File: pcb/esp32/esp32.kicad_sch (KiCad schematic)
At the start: 15 parts, among them J1 Conn_01x02_Female, J2 Conn_01x15_Female, J3 Screw_Terminal_01x02, J4 Conn_01x15_Female, J5 Conn_01x15_Female, J6 Conn_01x02_Female, J6der1 Conn_01x15_Female, J7 Conn_01x02_Female, J7der1 Conn_01x15_Female, J8 Conn_01x02_Female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

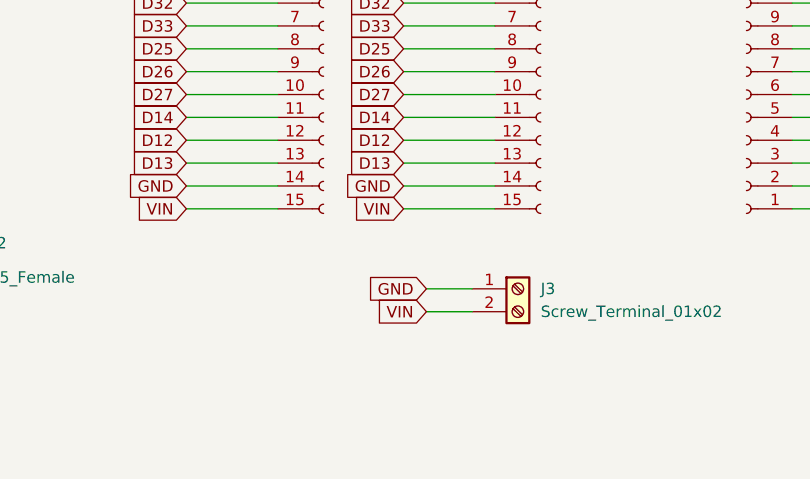
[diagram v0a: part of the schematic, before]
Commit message: added diode to esp32 board and updated solar board to fixed 5.0v ams1117
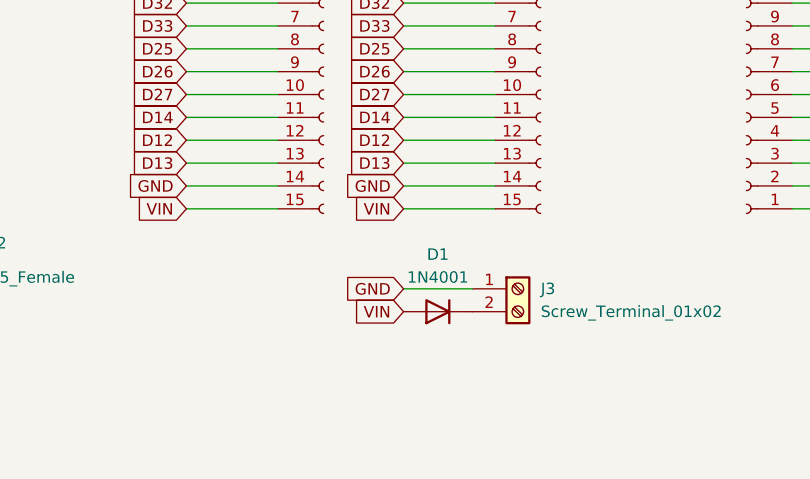
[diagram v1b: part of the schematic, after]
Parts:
- added D1: 1N4001, Diode_THT:D_DO-41_SOD81_P10.16mm_Horizontal, symbol Diode:1N4001
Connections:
- net VIN: now also D1.2 (A); no longer J3.2 (Pin_2)
- new net: D1.1 (K), J3.2 (Pin_2)
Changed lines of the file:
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@@
     (stroke (width 0) (type default) (color 0 0 0 0))
   )
-  (wire (pts (xy 121.92 97.79) (xy 127 97.79))
+  (wire (pts (xy 119.38 97.79) (xy 127 97.79))
     (stroke (width 0) (type default) (color 0 0 0 0))
   )
@@
     (stroke (width 0) (type default) (color 0 0 0 0))
   )
-  (wire (pts (xy 121.92 100.33) (xy 127 100.33))
-    (stroke (width 0) (type default) (color 0 0 0 0))
-  )
   (wire (pts (xy 57.15 63.5) (xy 67.31 63.5))
     (stroke (width 0) (type default) (color 0 0 0 0))
@@
     )
   )
-  (global_label "GND" (shape input) (at 121.92 97.79 180) (fields_autoplaced)
-    (effects (font (size 1.27 1.27)) (justify right))
-    (property "Intersheet References" "${INTERSHEET_REFS}" (id 0) (at 115.6364 97.7106 0)
+  (global_label "GND" (shape input) (at 119.38 97.79 180) (fields_autoplaced)
+    (effects (font (size 1.27 1.27)) (justify right))
+    (property "Intersheet References" "${INTERSHEET_REFS}" (id 0) (at 113.0964 97.7106 0)
       (effects (font (size 1.27 1.27)) (justify right) hide)
     )
@@
     )
   )
-  (global_label "VIN" (shape input) (at 121.92 100.33 180) (fields_autoplaced)
-    (effects (font (size 1.27 1.27)) (justify right))
-    (property "Intersheet References" "${INTERSHEET_REFS}" (id 0) (at 116.4831 100.2506 0)
+  (global_label "VIN" (shape input) (at 119.38 100.33 180) (fields_autoplaced)
+    (effects (font (size 1.27 1.27)) (justify right))
+    (property "Intersheet References" "${INTERSHEET_REFS}" (id 0) (at 113.9431 100.2506 0)
       (effects (font (size 1.27 1.27)) (justify right) hide)
     )
@@
     (pin "9")
   )
+  (symbol (lib_id "Diode:1N4001") (at 123.19 100.33 180) (unit 1)
+    (in_bom yes) (on_board yes) (fields_autoplaced)
+    (property "Reference" "D1" (id 0) (at 123.19 93.98 0))
+    (property "Value" "1N4001" (id 1) (at 123.19 96.52 0))
+    (property "Footprint" "Diode_THT:D_DO-41_SOD81_P10.16mm_Horizontal" (id 2) (at 123.19 95.885 0)
+      (effects (font (size 1.27 1.27)) hide)
+    )
+    (property "Datasheet" "http://www.vishay.com/docs/88503/1n4001.pdf" (id 3) (at 123.19 100.33 0)
+      (effects (font (size 1.27 1.27)) hide)
+    )
+    (pin "1")
+    (pin "2")
+  )
   (symbol (lib_id "Mechanical:MountingHole") (at 254 110.49 0) (unit 1)
     (in_bom yes) (on_board yes) (fields_autoplaced)
@@
   )
   (symbol_instances
+    (path "/5f59c1b8-50da-47fc-86f1-8013e6be9ffb"
+      (reference "D1") (unit 1) (value "1N4001") (footprint "Diode_THT:D_DO-41_SOD81_P10.16mm_Horizontal")
+    )
     (path "/90e39933-8cf6-43e9-82d7-37665a3a8f34"
       (reference "H1") (unit 1) (value "MountingHole") (footprint "MountingHole:MountingHole_2.1mm")

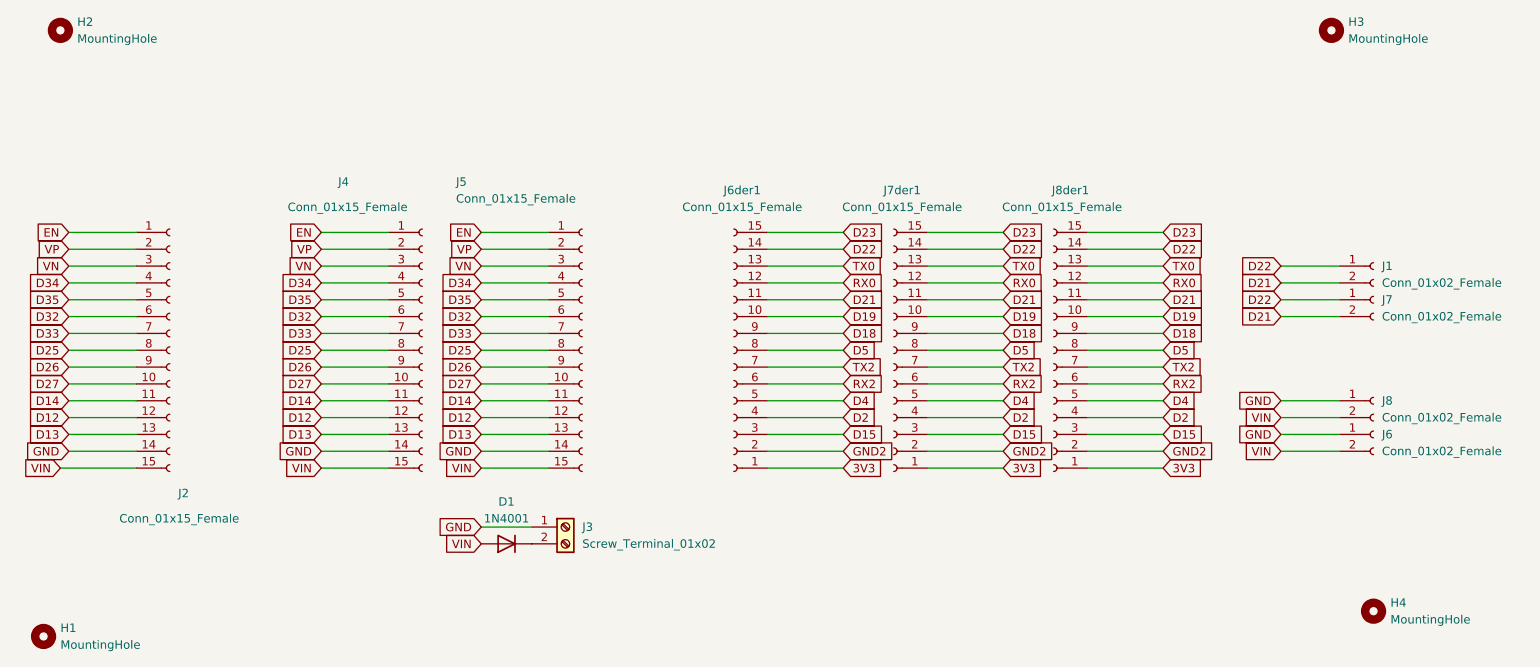
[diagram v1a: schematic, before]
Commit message: added new pins to connect more 3.3v sensors and 5.0v sensors, also added 2 pull up resistors for sda and scl pins
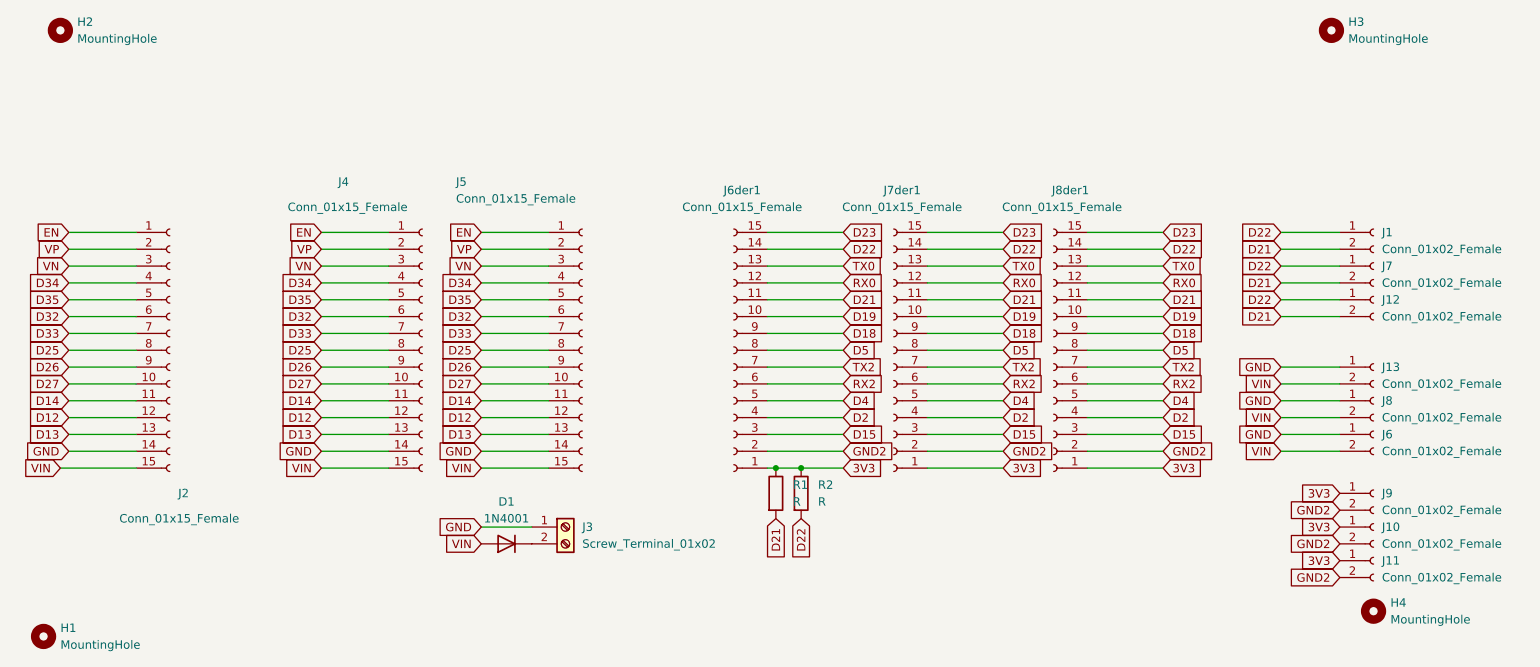
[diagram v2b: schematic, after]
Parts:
- added J10, J11, J12, J13, J9: Conn_01x02_Female, esp32_ur:Connector_Molex_Molex_SL_171971-0004_1x02_P2.54mm_Vertical_squares, symbol Connector:Conn_01x02_Female
- added R1: R, Resistor_THT:R_Axial_DIN0204_L3.6mm_D1.6mm_P5.08mm_Horizontal, symbol Device:R
- added R2: R, Resistor_THT:R_Axial_DIN0204_L3.6mm_D1.6mm_P7.62mm_Horizontal, symbol Device:R
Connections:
- net 3V3: now also J10.1 (Pin_1), J11.1 (Pin_1), J9.1 (Pin_1), R1.1, R2.1
- net D21: now also J12.2 (Pin_2), R1.2
- net D22: now also J12.1 (Pin_1), R2.2
- net GND: now also J13.1 (Pin_1)
- net GND2: now also J10.2 (Pin_2), J11.2 (Pin_2), J9.2 (Pin_2)
- net VIN: now also J13.2 (Pin_2)
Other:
- moved on the sheet: J1, J7

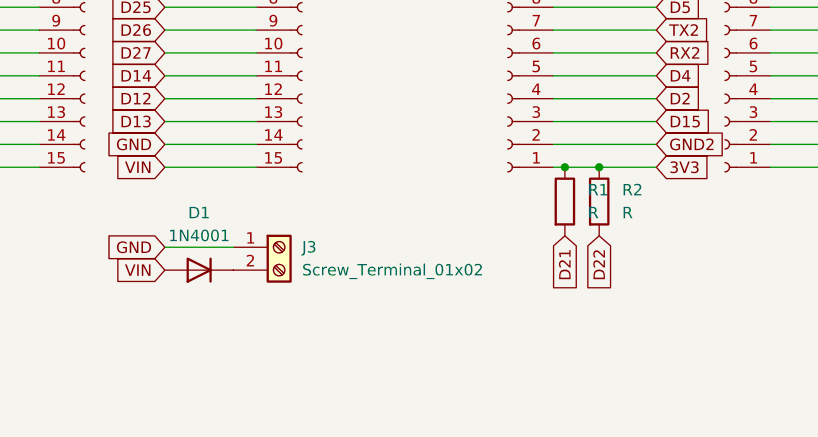
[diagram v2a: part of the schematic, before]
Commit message: changed the pull up from 5v to 3.3v
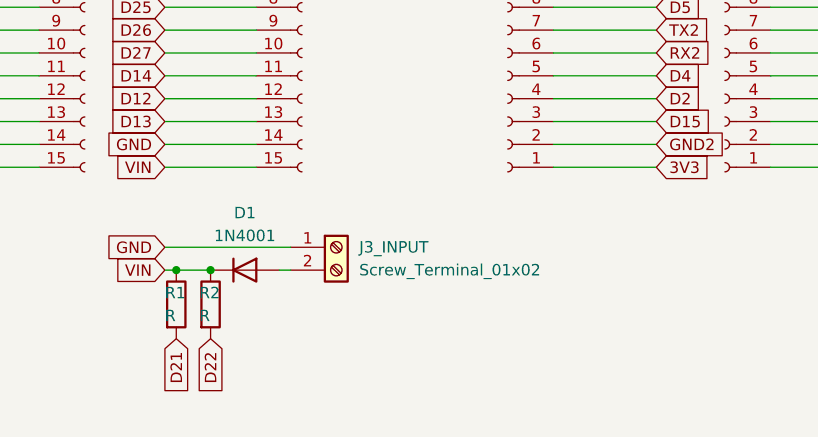
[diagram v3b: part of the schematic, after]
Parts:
- R1: footprint Resistor_THT:R_Axial_DIN0204_L3.6mm_D1.6mm_P5.08mm_Horizontal -> Resistor_THT:R_Axial_DIN0207_L6.3mm_D2.5mm_P15.24mm_Horizontal
- renumbered J3 to J3_INPUT
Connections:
- net 3V3: no longer R1.1, R2.1
- net VIN: now also D1.1 (K), R1.1, R2.1; no longer D1.2 (A)
- net at J3_INPUT.2 (Pin_2): now also D1.2 (A); no longer D1.1 (K)
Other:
- moved on the sheet: D1, J3_INPUT, R1, R2
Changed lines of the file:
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@@
 (kicad_sch (version 20211123) (generator eeschema)
   (paper "A4")
-  (junction (at 167.64 88.9) (diameter 0) (color 0 0 0 0)
-  )
-  (junction (at 163.83 88.9) (diameter 0) (color 0 0 0 0)
+  (junction (at 120.65 100.33) (diameter 0) (color 0 0 0 0)
+  )
+  (junction (at 124.46 100.33) (diameter 0) (color 0 0 0 0)
   )
   (wire (pts (xy 240.03 60.96) (xy 248.92 60.96))
@@
     (stroke (width 0) (type default) (color 0 0 0 0))
   )
-  (wire (pts (xy 162.56 88.9) (xy 163.83 88.9))
-    (stroke (width 0) (type default) (color 0 0 0 0))
-  )
   (wire (pts (xy 57.15 73.66) (xy 67.31 73.66))
     (stroke (width 0) (type default) (color 0 0 0 0))
@@
     (stroke (width 0) (type default) (color 0 0 0 0))
   )
+  (wire (pts (xy 120.65 100.33) (xy 124.46 100.33))
+    (stroke (width 0) (type default) (color 0 0 0 0))
+  )
   (wire (pts (xy 162.56 66.04) (xy 173.99 66.04))
     (stroke (width 0) (type default) (color 0 0 0 0))
@@
     (stroke (width 0) (type default) (color 0 0 0 0))
   )
-  (wire (pts (xy 119.38 97.79) (xy 127 97.79))
+  (wire (pts (xy 119.38 97.79) (xy 133.35 97.79))
     (stroke (width 0) (type default) (color 0 0 0 0))
   )
@@
     (stroke (width 0) (type default) (color 0 0 0 0))
   )
+  (wire (pts (xy 119.38 100.33) (xy 120.65 100.33))
+    (stroke (width 0) (type default) (color 0 0 0 0))
+  )
+  (wire (pts (xy 132.08 100.33) (xy 133.35 100.33))
+    (stroke (width 0) (type default) (color 0 0 0 0))
+  )
   (wire (pts (xy 119.38 76.2) (xy 129.54 76.2))
     (stroke (width 0) (type default) (color 0 0 0 0))
@@
     (stroke (width 0) (type default) (color 0 0 0 0))
   )
-  (wire (pts (xy 163.83 88.9) (xy 167.64 88.9))
-    (stroke (width 0) (type default) (color 0 0 0 0))
-  )
   (wire (pts (xy 119.38 73.66) (xy 129.54 73.66))
     (stroke (width 0) (type default) (color 0 0 0 0))
@@
     (stroke (width 0) (type default) (color 0 0 0 0))
   )
-  (wire (pts (xy 167.64 88.9) (xy 173.99 88.9))
+  (wire (pts (xy 162.56 88.9) (xy 173.99 88.9))
     (stroke (width 0) (type default) (color 0 0 0 0))
   )
@@
     )
   )
-  (global_label "D21" (shape input) (at 163.83 96.52 270) (fields_autoplaced)
-    (effects (font (size 1.27 1.27)) (justify right))
-    (property "Intersheet References" "${INTERSHEET_REFS}" (id 0) (at 163.9094 102.6221 90)
+  (global_label "D21" (shape input) (at 120.65 107.95 270) (fields_autoplaced)
+    (effects (font (size 1.27 1.27)) (justify right))
+    (property "Intersheet References" "${INTERSHEET_REFS}" (id 0) (at 120.7294 114.0521 90)
       (effects (font (size 1.27 1.27)) (justify right) hide)
     )
@@
     )
   )
-  (global_label "D22" (shape input) (at 167.64 96.52 270) (fields_autoplaced)
-    (effects (font (size 1.27 1.27)) (justify right))
-    (property "Intersheet References" "${INTERSHEET_REFS}" (id 0) (at 167.7194 102.6221 90)
+  (global_label "D22" (shape input) (at 124.46 107.95 270) (fields_autoplaced)
+    (effects (font (size 1.27 1.27)) (justify right))
+    (property "Intersheet References" "${INTERSHEET_REFS}" (id 0) (at 124.5394 114.0521 90)
       (effects (font (size 1.27 1.27)) (justify right) hide)
     )
@@
     (pin "9")
   )
-  (symbol (lib_id "Diode:1N4001") (at 123.19 100.33 180) (unit 1)
+  (symbol (lib_id "Diode:1N4001") (at 128.27 100.33 0) (unit 1)
     (in_bom yes) (on_board yes) (fields_autoplaced)
-    (property "Reference" "D1" (id 0) (at 123.19 93.98 0))
-    (property "Value" "1N4001" (id 1) (at 123.19 96.52 0))
-    (property "Footprint" "Diode_THT:D_DO-41_SOD81_P10.16mm_Horizontal" (id 2) (at 123.19 95.885 0)
-      (effects (font (size 1.27 1.27)) hide)
-    )
-    (property "Datasheet" "http://www.vishay.com/docs/88503/1n4001.pdf" (id 3) (at 123.19 100.33 0)
+    (property "Reference" "D1" (id 0) (at 128.27 93.98 0))
+    (property "Value" "1N4001" (id 1) (at 128.27 96.52 0))
+    (property "Footprint" "Diode_THT:D_DO-41_SOD81_P10.16mm_Horizontal" (id 2) (at 128.27 104.775 0)
+      (effects (font (size 1.27 1.27)) hide)
+    )
+    (property "Datasheet" "http://www.vishay.com/docs/88503/1n4001.pdf" (id 3) (at 128.27 100.33 0)
       (effects (font (size 1.27 1.27)) hide)
     )
@@
     )
   )
-  (symbol (lib_id "Device:R") (at 167.64 92.71 0) (unit 1)
-    (in_bom yes) (on_board yes) (fields_autoplaced)
-    (property "Reference" "R2" (id 0) (at 170.18 91.4399 0)
-      (effects (font (size 1.27 1.27)) (justify left))
-    )
-    (property "Value" "R" (id 1) (at 170.18 93.9799 0)
-      (effects (font (size 1.27 1.27)) (justify left))
-    )
-    (property "Footprint" "Resistor_THT:R_Axial_DIN0204_L3.6mm_D1.6mm_P7.62mm_Horizontal" (id 2) (at 165.862 92.71 90)
-      (effects (font (size 1.27 1.27)) hide)
-    )
-    (property "Datasheet" "~" (id 3) (at 167.64 92.71 0)
+  (symbol (lib_id "Device:R") (at 124.46 104.14 0) (unit 1)
+    (in_bom yes) (on_board yes)
+    (property "Reference" "R2" (id 0) (at 123.19 102.87 0)
+      (effects (font (size 1.27 1.27)) (justify left))
+    )
+    (property "Value" "R" (id 1) (at 123.19 105.41 0)
+      (effects (font (size 1.27 1.27)) (justify left))
+    )
+    (property "Footprint" "Resistor_THT:R_Axial_DIN0204_L3.6mm_D1.6mm_P7.62mm_Horizontal" (id 2) (at 122.682 104.14 90)
+      (effects (font (size 1.27 1.27)) hide)
+    )
+    (property "Datasheet" "~" (id 3) (at 124.46 104.14 0)
       (effects (font (size 1.27 1.27)) hide)
     )
@@
     (pin "2")
   )
-  (symbol (lib_id "Device:R") (at 163.83 92.71 0) (unit 1)
-    (in_bom yes) (on_board yes) (fields_autoplaced)
-    (property "Reference" "R1" (id 0) (at 166.37 91.4399 0)
-      (effects (font (size 1.27 1.27)) (justify left))
-    )
-    (property "Value" "R" (id 1) (at 166.37 93.9799 0)
-      (effects (font (size 1.27 1.27)) (justify left))
-    )
-    (property "Footprint" "Resistor_THT:R_Axial_DIN0204_L3.6mm_D1.6mm_P5.08mm_Horizontal" (id 2) (at 162.052 92.71 90)
-      (effects (font (size 1.27 1.27)) hide)
-    )
-    (property "Datasheet" "~" (id 3) (at 163.83 92.71 0)
+  (symbol (lib_id "Device:R") (at 120.65 104.14 0) (unit 1)
+    (in_bom yes) (on_board yes)
+    (property "Reference" "R1" (id 0) (at 119.38 102.87 0)
+      (effects (font (size 1.27 1.27)) (justify left))
+    )
+    (property "Value" "R" (id 1) (at 119.38 105.41 0)
+      (effects (font (size 1.27 1.27)) (justify left))
+    )
+    (property "Footprint" "Resistor_THT:R_Axial_DIN0207_L6.3mm_D2.5mm_P15.24mm_Horizontal" (id 2) (at 118.872 104.14 90)
+      (effects (font (size 1.27 1.27)) hide)
+    )
+    (property "Datasheet" "~" (id 3) (at 120.65 104.14 0)
       (effects (font (size 1.27 1.27)) hide)
     )
@@
     )
   )
-  (symbol (lib_id "Connector:Screw_Terminal_01x02") (at 132.08 97.79 0) (unit 1)
+  (symbol (lib_id "Connector:Screw_Terminal_01x02") (at 138.43 97.79 0) (unit 1)
     (in_bom yes) (on_board yes) (fields_autoplaced)
-    (property "Reference" "J3" (id 0) (at 134.62 97.7899 0)
-      (effects (font (size 1.27 1.27)) (justify left))
-    )
-    (property "Value" "Screw_Terminal_01x02" (id 1) (at 134.62 100.3299 0)
-      (effects (font (size 1.27 1.27)) (justify left))
-    )
-    (property "Footprint" "TerminalBlock_MetzConnect:TerminalBlock_MetzConnect_Type055_RT01502HDWU_1x02_P5.00mm_Horizontal" (id 2) (at 132.08 97.79 0)
-      (effects (font (size 1.27 1.27)) hide)
-    )
-    (property "Datasheet" "~" (id 3) (at 132.08 97.79 0)
+    (property "Reference" "J3_INPUT" (id 0) (at 140.97 97.7899 0)
+      (effects (font (size 1.27 1.27)) (justify left))
+    )
+    (property "Value" "Screw_Terminal_01x02" (id 1) (at 140.97 100.3299 0)
+      (effects (font (size 1.27 1.27)) (justify left))
+    )
+    (property "Footprint" "TerminalBlock_MetzConnect:TerminalBlock_MetzConnect_Type055_RT01502HDWU_1x02_P5.00mm_Horizontal" (id 2) (at 138.43 97.79 0)
+      (effects (font (size 1.27 1.27)) hide)
+    )
+    (property "Datasheet" "~" (id 3) (at 138.43 97.79 0)
       (effects (font (size 1.27 1.27)) hide)
     )
@@
     )
     (path "/dadb3456-66e9-4f2d-b628-b398dec30885"
-      (reference "J3") (unit 1) (value "Screw_Terminal_01x02") (footprint "TerminalBlock_MetzConnect:TerminalBlock_MetzConnect_Type055_RT01502HDWU_1x02_P5.00mm_Horizontal")
+      (reference "J3_INPUT") (unit 1) (value "Screw_Terminal_01x02") (footprint "TerminalBlock_MetzConnect:TerminalBlock_MetzConnect_Type055_RT01502HDWU_1x02_P5.00mm_Horizontal")
     )
     (path "/2cea8539-aba7-40d0-8602-11aebc571d08"
@@
     )
     (path "/88941c6c-4802-4323-a942-795e7ad1d8f0"
-      (reference "R1") (unit 1) (value "R") (footprint "Resistor_THT:R_Axial_DIN0204_L3.6mm_D1.6mm_P5.08mm_Horizontal")
+      (reference "R1") (unit 1) (value "R") (footprint "Resistor_THT:R_Axial_DIN0207_L6.3mm_D2.5mm_P15.24mm_Horizontal")
     )
     (path "/71a2e461-9fbc-44c1-a14c-c6ba2b291653"
